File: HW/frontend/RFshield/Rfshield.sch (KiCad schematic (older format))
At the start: 139 parts, among them P1 BASEBAND, P10 TXENABLE, P11 RXENABLE, P12 XTAL2, P13 GCK1, P14 GCK2, P15 SGPIO_CLK, P16 DA0, P17 DA4, P18 DA7, P19 DD0, P2 VAA, P20 DD5, P21 DD9, P22 RSSI, P23 GND, P24 GND, P25 GND, P26 GND, P27 GND, P28 GND, P29 GND, P3 SCL, P30 GND, P31 GND, P32 GND, P33 XCVR_CLKOUT, P34 CONN_02X14, P35 CONN_02X13, P36 CONN_02X18, P37 INTR, P38 CLKIN, P39 CLKOUT, P4 SDA, P40 OEB, P5 SSP1_SCK, P6 SSP1_MOSI, P7 SSP1_MISO, P8 CS_XCVR, P9 CS_AD, Q1 MOSFET_P, T1 RX_BALUN, T2 TX_BALUN, U1 MAX2837, U2 MAX5864, U3 SI5351C, X1 GSG-XTAL4PIN

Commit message: schematic spi i2c connections
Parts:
- renumbered P36 to PFIO1, P35 to PFIO2, P34 to PSA1
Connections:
- wire segments 385 -> 399
- no-connect marks 10 -> 11
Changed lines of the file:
@@
 	6700 6700 6700 6850
 Wire Wire Line
-	6700 7900 6700 7800
+	6700 7750 6700 7900
 Wire Wire Line
 	4200 1250 4200 1400
@@
 	2500 7750 2500 7950
 Wire Wire Line
-	11650 5900 11650 6000
+	11650 5850 11650 6000
 Wire Wire Line
 	11150 5850 11150 6000
@@
 Connection ~ 11950 4300
 Wire Wire Line
-	11650 5500 11650 4300
+	11650 4300 11650 5550
 Connection ~ 11650 4300
 Connection ~ 2500 7950
@@
 	8350 8550 8350 8700
 Wire Wire Line
-	7650 9000 7650 9100
+	7650 8950 7650 9100
 Wire Wire Line
 	6700 9100 7000 9100
@@
 	16200 7100 16200 7050
 $Comp
-L CONN_02X13 P35
+L CONN_02X13 PFIO2
 U 1 1 55A59163
 P 10850 7800
-F 0 "P35" H 10850 8500 50  0000 C CNN
+F 0 "PFIO2" H 10850 8500 50  0000 C CNN
 F 1 "CONN_02X13" V 10850 7800 50  0000 C CNN
 F 2 "" H 10850 6650 60  0001 C CNN
@@
 $EndComp
 $Comp
-L CONN_02X14 P34
+L CONN_02X14 PSA1
 U 1 1 55A592FE
 P 12700 7750
-F 0 "P34" H 12700 8500 50  0000 C CNN
+F 0 "PSA1" H 12700 8500 50  0000 C CNN
 F 1 "CONN_02X14" V 12700 7750 50  0000 C CNN
 F 2 "" H 12700 6600 60  0001 C CNN
@@
 $EndComp
 $Comp
-L CONN_02X18 P36
+L CONN_02X18 PFIO1
 U 1 1 55A594A9
 P 14500 7850
-F 0 "P36" H 14500 8800 50  0000 C CNN
+F 0 "PFIO1" H 14500 8800 50  0000 C CNN
 F 1 "CONN_02X18" V 14500 7850 50  0000 C CNN
 F 2 "" H 14500 6800 60  0001 C CNN
@@
 	1    0    0    -1
 $EndComp
+Text GLabel 14900 8000 2    40   Input ~ 0
+DA7
+Text GLabel 14900 8100 2    40   Input ~ 0
+DA6
+Text GLabel 14900 8200 2    40   Input ~ 0
+DA5
+Text GLabel 14900 8300 2    40   Input ~ 0
+DA4
+Text GLabel 14900 8400 2    40   Input ~ 0
+DA3
+Text GLabel 14900 8500 2    40   Input ~ 0
+DA2
+Text GLabel 14900 8600 2    40   Input ~ 0
+DA1
+Text GLabel 14900 8700 2    40   Input ~ 0
+DA0
+Text GLabel 14900 7000 2    40   Input ~ 0
+DD0
+Text GLabel 14900 7100 2    40   Input ~ 0
+DD1
 Text GLabel 14900 7200 2    40   Input ~ 0
-DA7
+DD2
 Text GLabel 14900 7300 2    40   Input ~ 0
-DA6
+DD3
 Text GLabel 14900 7400 2    40   Input ~ 0
-DA5
+DD4
 Text GLabel 14900 7500 2    40   Input ~ 0
-DA4
+DD5
+Text GLabel 14900 7600 2    40   Input ~ 0
+DD6
+Text GLabel 14900 7700 2    40   Input ~ 0
+DD7
 Text GLabel 14900 7800 2    40   Input ~ 0
-DA3
+DD8
 Text GLabel 14900 7900 2    40   Input ~ 0
-DA2
-Text GLabel 14900 8000 2    40   Input ~ 0
-DA1
-Text GLabel 14900 8100 2    40   Input ~ 0
-DA0
-Text GLabel 14900 7100 2    40   Input ~ 0
-DD0
-Text GLabel 14900 7000 2    40   Input ~ 0
-DD1
+DD9
+NoConn ~ 15350 7300
 Wire Wire Line
 	14750 7000 14900 7000
@@
 Wire Wire Line
 	14750 7500 14900 7500
+Wire Wire Line
+	14750 7600 14900 7600
+Wire Wire Line
+	14750 7700 14900 7700
+Wire Wire Line
+	14750 7800 14900 7800
+Wire Wire Line
+	14750 7900 14900 7900
+Wire Wire Line
+	14750 8000 14900 8000
+Wire Wire Line
+	14750 8100 14900 8100
+Wire Wire Line
+	14750 8200 14900 8200
+Wire Wire Line
+	14750 8300 14900 8300
+Wire Wire Line
+	14750 8400 14900 8400
+Wire Wire Line
+	14750 8500 14900 8500
+Wire Wire Line
+	14750 8600 14900 8600
+Wire Wire Line
+	14750 8700 14900 8700
+Text GLabel 10450 7200 0    40   Input ~ 0
+CS_AD
+Text GLabel 10450 7300 0    40   Input ~ 0
+SSP1_SCK
+Text GLabel 10450 7400 0    40   Input ~ 0
+SSP1_MOSI
+Text GLabel 12300 8000 0    40   Input ~ 0
+SDA
+Text GLabel 13050 7700 2    40   Input ~ 0
+SCL
+Wire Wire Line
+	13050 7700 12950 7700
+Wire Wire Line
+	12300 8000 12450 8000
+Text GLabel 10450 7700 0    40   Input ~ 0
+CS_XCVR
+Text GLabel 10450 7500 0    40   Input ~ 0
+RSSI
+Text GLabel 10450 7600 0    40   Input ~ 0
+SSP1_MOSI
+Text GLabel 10450 7800 0    40   Input ~ 0
+SSP1_MISO
 $EndSCHEMATC

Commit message: schematic connections checked and finished
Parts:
- removed PFIO2: CONN_02X13, symbol CONN_02X13
- added 22pF1: C_Small, Capacitors_SMD:C_0402, symbol C_Small
- added GndCon1: GND, Connect:1pin, symbol CONN_1
- added PFIO2: CONN_02X12, symbol CONN_02X12
- added R26: 0, symbol R
- added RX1, TX1: GSG-SMA-CONN, symbol GSG-SMA-CONN
- C25, C26, C27, C28, C29, C30, C31, C32, C33, C34, C35, C36, C37, C38, C39, C40, C41, C42, C43, C44, C45, C46, C47, C48, C49, C50, C51, C52, C53, C54, C55, C56, C57, C58, C59, D1, D2: footprint (none) -> Capacitors_SMD:C_0402
- C60: footprint (none) -> Capacitors_SMD:C_0603
- FB1: footprint (none) -> Capacitors_SMD:C_0805
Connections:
- wire segments 399 -> 435
- no-connect marks 11 -> 68
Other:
- note added: "2 chip select input for spi"
- note added: "ground connector from basic pcb"
- note added: "transceiver\n logic pins\n"
- moved on the sheet: PSA1

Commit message: board file generated, routing in process
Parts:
- removed P1: BASEBAND, symbol CONN_8X2
- removed P40: OEB, symbol CONN_1
- removed RX1, TX1: GSG-SMA-CONN, symbol GSG-SMA-CONN
- added RX1, TX1: CLKOUT, hackrf1:GSG-SMA-EDGE, symbol GSG-RF-CONN
- L1, L2, L3, L4: footprint (none) -> Capacitors_SMD:C_0402
- P10, P11, P12, P13, P14, P15, P16, P17, P18, P19, P20, P21, P22, P23, P24, P25, P26, P27, P28, P29, P3, P30, P31, P32, P33, P37, P4, P5, P6, P7, P8, P9: footprint (none) -> hackrf1:GSG-TESTPOINT-50MIL-MASKONLY
- P2: footprint (none) -> Pin_Headers:Pin_Header_Straight_1x02_Pitch3.96mm_Friction_Lock
- P38, P39: footprint (none) -> hackrf1:GSG-SMA-73251-2120
- PFIO1: footprint (none) -> Socket_Strips:Socket_Strip_Straight_2x18
- PFIO2: footprint (none) -> Socket_Strips:Socket_Strip_Straight_2x12
- PSA1: footprint (none) -> Socket_Strips:Socket_Strip_Straight_2x14
- Q1: footprint (none) -> kicad1:SOT-23mos
- R1, R10, R11, R12, R13, R14, R15, R16, R17, R18, R19, R2, R20, R21, R22, R23, R24, R25, R26, R3, R4, R5, R6, R7, R8, R9: footprint (none) -> Resistors_SMD:R_0402
- T1, T2: footprint (none) -> hackrf1:GSG-2500BL14M100
- U1: footprint (none) -> hackrf1:GSG-QFN48-6
- U2: footprint (none) -> hackrf1:GSG-QFN48-7
- U3: footprint (none) -> hackrf1:GSG-QFN20-4
- X1: footprint (none) -> hackrf1:GSG-XTAL3.2x2.5mm
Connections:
- net GND: now also RX1.2 (GND), TX1.2 (GND)
- net OEB: now also PSA1.21 (P21)
- net RX_IF: now also RX1.1 (RF)
- net at 22pF1.2: now also TX1.1 (RF)
- no-connect marks 68 -> 67

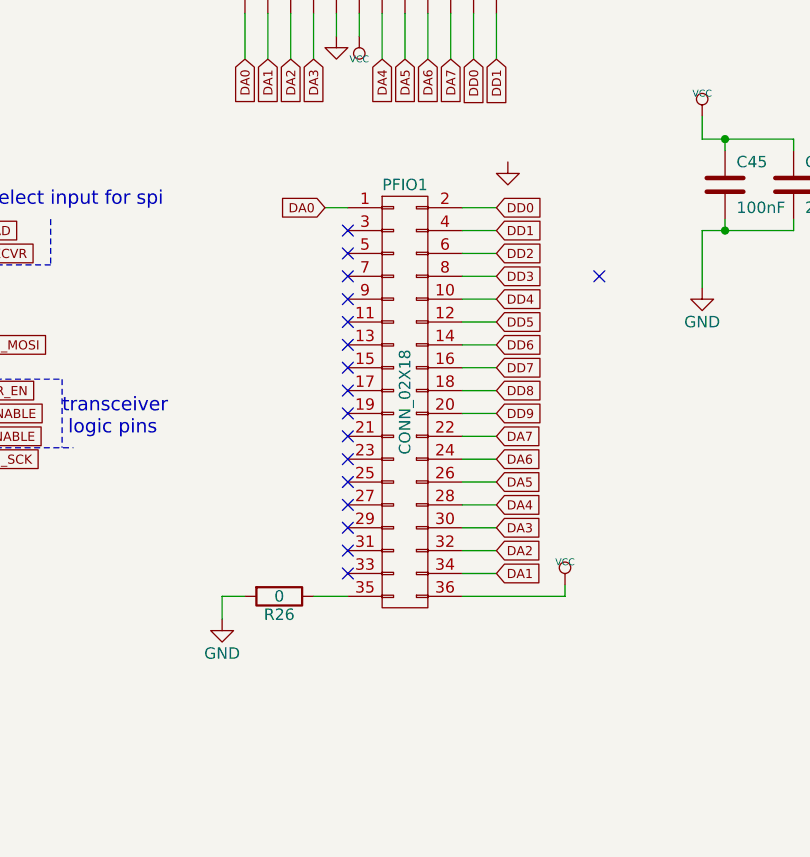
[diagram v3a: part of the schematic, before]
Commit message: last changes
all components placed, routes traced, ground shields missing
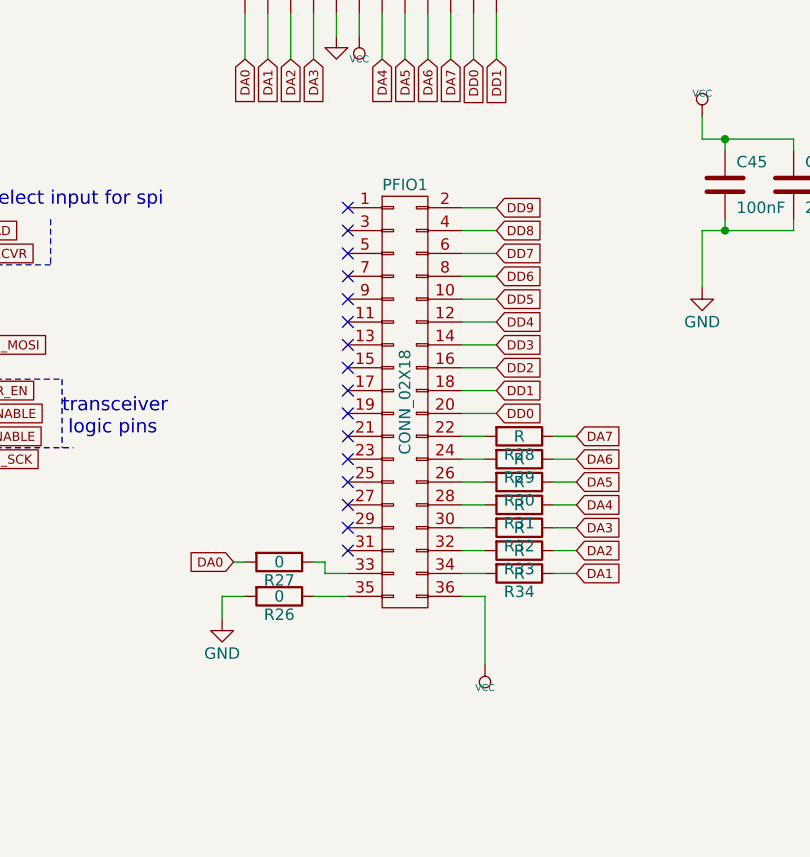
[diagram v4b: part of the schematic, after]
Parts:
- added R27: 0, hackrf1:GSG-0402, symbol R
- added R28, R29, R30, R31, R32, R33, R34: R, hackrf1:GSG-0402, symbol R
- 22pF1, C1, C10, C11, C12, C13, C14, C15, C16, C17, C18, C19, C2, C20, C21, C22, C23, C24, C25, C26, C27, C28, C29, C3, C30, C31, C32, C33, C34, C35, C36, C37, C38, C39, C4, C40, C41, C42, C43, C44, C45, C46, C47, C48, C49, C5, C50, C51, C52, C53, C54, C55, C56, C57, C58, C59, C6, C7, C8, C9, D1, D2, L1, L2, L3, L4: footprint Capacitors_SMD:C_0402 -> hackrf1:GSG-0402
- C60: footprint Capacitors_SMD:C_0603 -> hackrf1:GSG-0603
- FB1: footprint Capacitors_SMD:C_0805 -> hackrf1:GSG-0805
- P10, P11, P12, P13, P14, P15, P16, P17, P18, P19, P20, P21, P22, P23, P24, P25, P26, P27, P28, P29, P3, P30, P31, P32, P33, P37, P4, P5, P6, P7, P8, P9: footprint hackrf1:GSG-TESTPOINT-50MIL-MASKONLY -> hackrf1:GSG-TESTPOINT-30MIL-MASKONLY
- P38, P39: footprint hackrf1:GSG-SMA-73251-2120 -> hackrf1:GSG-SMA-EDGE
- R1, R10, R11, R12, R13, R14, R15, R16, R17, R18, R19, R2, R20, R21, R22, R23, R24, R25, R26, R3, R4, R5, R6, R7, R8, R9: footprint Resistors_SMD:R_0402 -> hackrf1:GSG-0402
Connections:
- net DA0: now also R27.2; no longer PFIO1.1 (P1)
- net DA1: now also R34.1; no longer PFIO1.34 (P34)
- net DA2: now also R33.1; no longer PFIO1.32 (P32)
- net DA3: now also R32.1; no longer PFIO1.30 (P30)
- net DA4: now also R31.1; no longer PFIO1.28 (P28)
- net DA5: now also R30.1; no longer PFIO1.26 (P26)
- net DA6: now also R29.1; no longer PFIO1.24 (P24)
- net DA7: now also R28.1; no longer PFIO1.22 (P22)
- net DD0: now also PFIO1.20 (P20); no longer PFIO1.2 (P2)
- net DD1: now also PFIO1.18 (P18); no longer PFIO1.4 (P4)
- net DD2: now also PFIO1.16 (P16); no longer PFIO1.6 (P6)
- net DD3: now also PFIO1.14 (P14); no longer PFIO1.8 (P8)
- net DD4: now also PFIO1.12 (P12); no longer PFIO1.10 (P10)
- net DD5: now also PFIO1.10 (P10); no longer PFIO1.12 (P12)
- net DD6: now also PFIO1.8 (P8); no longer PFIO1.14 (P14)
- net DD7: now also PFIO1.6 (P6); no longer PFIO1.16 (P16)
- net DD8: now also PFIO1.4 (P4); no longer PFIO1.18 (P18)
- net DD9: now also PFIO1.2 (P2); no longer PFIO1.20 (P20)
- net at PFIO1.33 (P33): now also R27.1
- new net: PFIO1.22 (P22), R28.2
- new net: PFIO1.24 (P24), R29.2
- new net: PFIO1.26 (P26), R30.2
- new net: PFIO1.28 (P28), R31.2
- new net: PFIO1.30 (P30), R32.2
- new net: PFIO1.32 (P32), R33.2
- new net: PFIO1.34 (P34), R34.2
- no-connect marks 67 -> 66

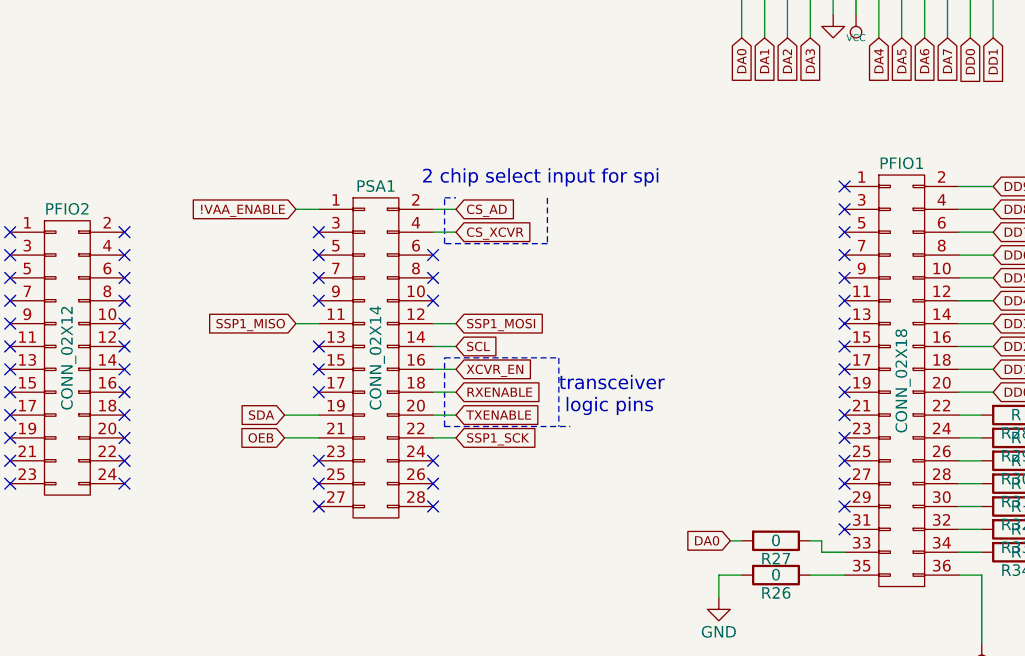
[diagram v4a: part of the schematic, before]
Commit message: shunt componnents grounded
ground vias placed in shunt components
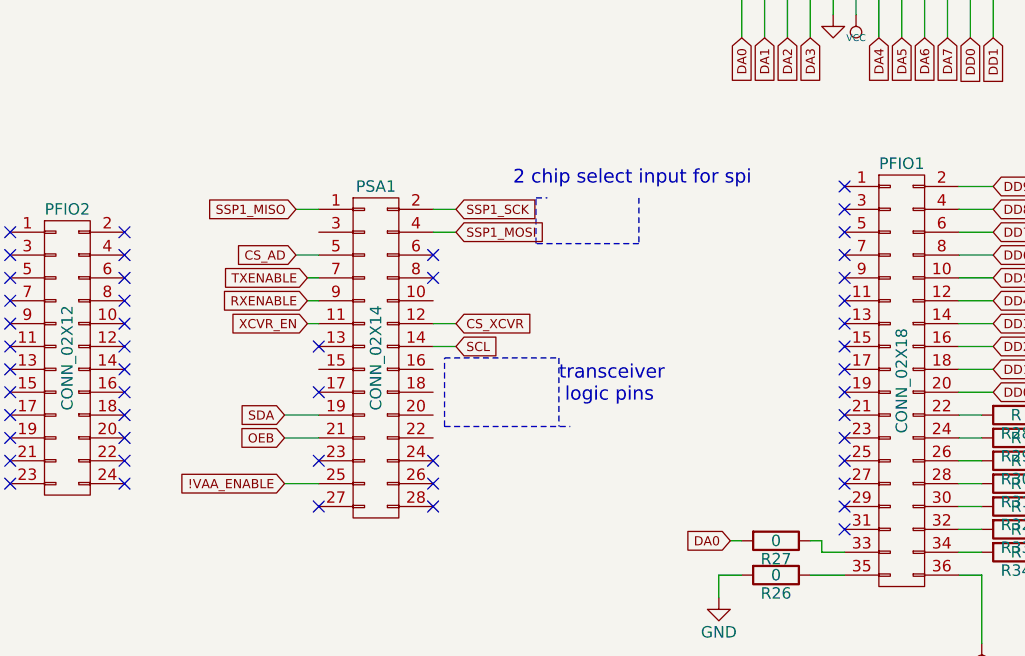
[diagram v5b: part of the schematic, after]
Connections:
- net !VAA_ENABLE: now also PSA1.25 (P25); no longer PSA1.1 (P1)
- net CS_AD: now also PSA1.5 (P5); no longer PSA1.2 (P2)
- net CS_XCVR: now also PSA1.12 (P12); no longer PSA1.4 (P4)
- net RXENABLE: now also PSA1.9 (P9); no longer PSA1.18 (P18)
- net SSP1_MISO: now also PSA1.1 (P1); no longer PSA1.11 (P11)
- net SSP1_MOSI: now also PSA1.4 (P4); no longer PSA1.12 (P12)
- net SSP1_SCK: now also PSA1.2 (P2); no longer PSA1.22 (P22)
- net TXENABLE: now also PSA1.7 (P7); no longer PSA1.20 (P20)
- net XCVR_EN: now also PSA1.11 (P11); no longer PSA1.16 (P16)
- no-connect marks 66 -> 59
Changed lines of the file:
@@
 Text GLabel 12550 7700 2    40   Input ~ 0
 SCL
+Text GLabel 12550 7600 2    40   Input ~ 0
+CS_XCVR
 Text GLabel 12550 7200 2    40   Input ~ 0
-CS_XCVR
-Text GLabel 12550 7600 2    40   Input ~ 0
 SSP1_MOSI
-Text GLabel 11850 7600 0    40   Input ~ 0
+Text GLabel 11850 7100 0    40   Input ~ 0
 SSP1_MISO
-Text GLabel 12550 8100 2    40   Input ~ 0
+Text GLabel 12550 7100 2    40   Input ~ 0
 SSP1_SCK
 $Comp
@@
 	1    0    0    -1
 $EndComp
-Text GLabel 12550 7800 2    40   Input ~ 0
+Text GLabel 11900 7600 0    40   Input ~ 0
 XCVR_EN
-Text GLabel 12550 8000 2    40   Input ~ 0
+Text GLabel 11900 7400 0    40   Input ~ 0
 TXENABLE
-Text GLabel 12550 7900 2    40   Input ~ 0
+Text GLabel 11900 7500 0    40   Input ~ 0
 RXENABLE
-Text GLabel 12550 7100 2    40   Input ~ 0
+Text GLabel 11850 7300 0    40   Input ~ 0
 CS_AD
-Text Notes 12400 7000 0    60   ~ 0
+Text Notes 12800 7000 0    60   ~ 0
 2 chip select input for spi
-Text Notes 13000 8000 0    60   ~ 0
+Text Notes 13000 7950 0    60   ~ 0
 transceiver\n logic pins\n
 NoConn ~ 11100 7200
@@
 Wire Wire Line
 	11800 8000 11950 8000
-Wire Wire Line
-	11850 7600 11950 7600
-Wire Wire Line
-	12550 7100 12450 7100
-Wire Wire Line
-	12550 7200 12450 7200
-Wire Wire Line
-	12550 7600 12450 7600
-Wire Wire Line
-	12550 8100 12450 8100
 Wire Notes Line
-	12950 7050 12950 7250
+	13350 7050 13350 7250
 Wire Notes Line
-	12950 7250 12500 7250
+	13350 7250 12900 7250
 Wire Notes Line
-	12500 7250 12500 7050
+	12900 7250 12900 7050
 Wire Notes Line
-	12500 7050 12550 7050
+	12900 7050 12950 7050
 Wire Notes Line
 	13000 7750 13000 8050
@@
 Wire Notes Line
 	12500 7750 13000 7750
-Wire Wire Line
-	12550 7800 12450 7800
-Wire Wire Line
-	12550 7900 12450 7900
-Wire Wire Line
-	12550 8000 12450 8000
 $Comp
 L GND #PWR095
@@
 Wire Wire Line
 	14100 8700 14250 8700
-NoConn ~ 11950 7200
-NoConn ~ 11950 7300
-NoConn ~ 11950 7400
-NoConn ~ 11950 7500
 NoConn ~ 12450 7300
 NoConn ~ 12450 7400
-NoConn ~ 12450 7500
 NoConn ~ 11950 7700
-NoConn ~ 11950 7800
 NoConn ~ 11950 7900
 NoConn ~ 11950 8200
-NoConn ~ 11950 8300
 NoConn ~ 11950 8400
 NoConn ~ 12450 8200
@@
 Wire Wire Line
 	15800 1300 15800 1400
-Text GLabel 11850 7100 0    40   Input ~ 0
+Text GLabel 11800 8300 0    40   Input ~ 0
 !VAA_ENABLE
-Wire Wire Line
-	11850 7100 11950 7100
 Wire Wire Line
 	11700 950  11700 900
@@
 Wire Wire Line
 	14150 8600 14250 8600
+Wire Wire Line
+	11850 7100 11950 7100
+Wire Wire Line
+	12550 7100 12450 7100
+Wire Wire Line
+	12550 7200 12450 7200
+Wire Wire Line
+	11800 8300 11950 8300
+Wire Wire Line
+	11850 7300 11950 7300
+Wire Wire Line
+	11900 7400 11950 7400
+Wire Wire Line
+	11900 7500 11950 7500
+Wire Wire Line
+	11900 7600 11950 7600
+Wire Wire Line
+	12450 7600 12550 7600
 $EndSCHEMATC
